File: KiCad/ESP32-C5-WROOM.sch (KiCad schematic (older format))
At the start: 4 parts, among them J14 USB_C_Receptacle_USB2.0, U13 ESP32-C5-WROOM-1U-N8R8

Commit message: Change R4 to 0603 and route the SD_LED circuit, add push-button for ESP32-C5 BOOT functionality (BT3)
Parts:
- added BT3: BT_Push, SF2000:Sunrom_Tactile_Switch_3x4x2mm_SMD_2-Pin, symbol Switch:SW_Push
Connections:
- net GND: now also BT3.1
- net at U13.15 (IO28): now also BT3.2
- no-connect marks 20 -> 19
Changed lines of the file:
@@
 NoConn ~ 1650 2550
 NoConn ~ 1650 2650
-NoConn ~ 1650 2950
 NoConn ~ 1650 3050
 NoConn ~ 1650 3150
 NoConn ~ 1650 3250
 NoConn ~ 1650 3350
+$Comp
+L Switch:SW_Push BT?
+U 1 1 6B13C84E
+P 950 2950
+AR Path="/6AFE5B10/6B13C84E" Ref="BT?"  Part="1"
+AR Path="/6AB92870/6B13C84E" Ref="BT3"  Part="1"
+F 0 "BT3" H 950 3235 50  0000 C CNN
+F 1 "BT_Push" H 950 3144 50  0000 C CNN
+F 2 "SF2000:Sunrom_Tactile_Switch_3x4x2mm_SMD_2-Pin" H 950 3150 50  0001 C CNN
+F 3 "~" H 950 3150 50  0001 C CNN
+	1    950  2950
+	1    0    0    -1
+$EndComp
+Text GLabel 750  2950 0    50   Input ~ 0
+GND
+Wire Wire Line
+	1650 2950 1150 2950
 $EndSCHEMATC

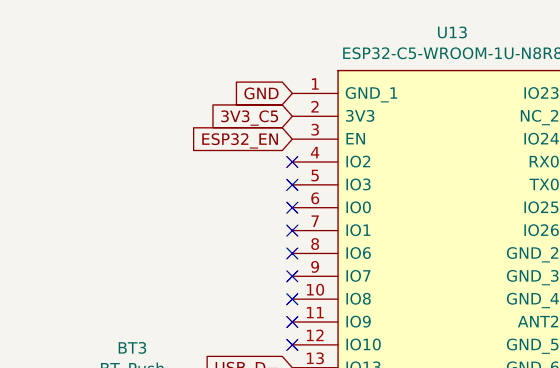
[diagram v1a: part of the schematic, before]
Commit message: Add BT4 push-button for RESET on the EN-signal for the ESP32-C5
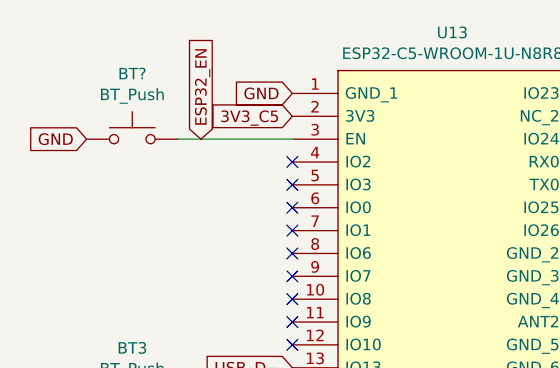
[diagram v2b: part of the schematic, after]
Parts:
- added BT?: BT_Push, SF2000:Sunrom_Tactile_Switch_3x4x2mm_SMD_2-Pin, symbol Switch:SW_Push
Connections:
- net ESP32_EN: now also BT?.2
- net GND: now also BT?.1
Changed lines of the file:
@@
 Text GLabel 3050 1550 2    50   Output ~ 0
 ESP32_TX1
-Text GLabel 1650 1750 0    50   Input ~ 0
+Text GLabel 1250 1750 1    50   Input ~ 0
 ESP32_EN
 NoConn ~ 3050 2550
@@
 Wire Wire Line
 	1650 2950 1150 2950
+$Comp
+L Switch:SW_Push BT?
+U 1 1 6B1C0633
+P 950 1750
+AR Path="/6AFE5B10/6B1C0633" Ref="BT?"  Part="1"
+AR Path="/6AB92870/6B1C0633" Ref="BT?"  Part="1"
+F 0 "BT?" H 950 2035 50  0000 C CNN
+F 1 "BT_Push" H 950 1944 50  0000 C CNN
+F 2 "SF2000:Sunrom_Tactile_Switch_3x4x2mm_SMD_2-Pin" H 950 1950 50  0001 C CNN
+F 3 "~" H 950 1950 50  0001 C CNN
+	1    950  1750
+	1    0    0    -1
+$EndComp
+Text GLabel 750  1750 0    50   Input ~ 0
+GND
+Wire Wire Line
+	1650 1750 1150 1750
 $EndSCHEMATC

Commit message: Change C15 to 0603 and use it for ESP32-C5 EN-signal, add 10k pull-up resistor (R24) on EN-signal
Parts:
- added C15: 0.1uF, Capacitor_SMD:C_0603_1608Metric_Pad1.08x0.95mm_HandSolder, symbol Device:C
- added R24: 10k, Resistor_SMD:R_0603_1608Metric_Pad0.98x0.95mm_HandSolder, symbol Device:R_Small
- gave numbers to parts that had none: 1
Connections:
- net ESP32_EN: now also C15.1, R24.1
- net GND: now also C15.2
- new net 3V3: R24.2
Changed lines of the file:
@@
 P 950 1750
 AR Path="/6AFE5B10/6B1C0633" Ref="BT?"  Part="1"
-AR Path="/6AB92870/6B1C0633" Ref="BT?"  Part="1"
-F 0 "BT?" H 950 2035 50  0000 C CNN
+AR Path="/6AB92870/6B1C0633" Ref="BT4"  Part="1"
+F 0 "BT4" H 950 2035 50  0000 C CNN
 F 1 "BT_Push" H 950 1944 50  0000 C CNN
 F 2 "SF2000:Sunrom_Tactile_Switch_3x4x2mm_SMD_2-Pin" H 950 1950 50  0001 C CNN
@@
 GND
 Wire Wire Line
-	1650 1750 1150 1750
+	1650 1750 1400 1750
+$Comp
+L Device:C C?
+U 1 1 6B1E6F7D
+P 1400 1900
+AR Path="/6B1E6F7D" Ref="C?"  Part="1"
+AR Path="/620D263D/6B1E6F7D" Ref="C?"  Part="1"
+AR Path="/6AB92870/6B1E6F7D" Ref="C15"  Part="1"
+F 0 "C15" H 1450 2000 50  0000 L CNN
+F 1 "0.1uF" H 1400 1800 50  0000 L CNN
+F 2 "Capacitor_SMD:C_0603_1608Metric_Pad1.08x0.95mm_HandSolder" H 1438 1750 50  0001 C CNN
+F 3 "~" H 1400 1900 50  0001 C CNN
+	1    1400 1900
+	1    0    0    -1
+$EndComp
+Text GLabel 1400 2050 3    50   Input ~ 0
+GND
+$Comp
+L Device:R_Small R?
+U 1 1 6B1F631E
+P 1150 1850
+AR Path="/6B1F631E" Ref="R?"  Part="1"
+AR Path="/6AFE5B10/6B1F631E" Ref="R?"  Part="1"
+AR Path="/6AB92870/6B1F631E" Ref="R24"  Part="1"
+F 0 "R24" H 1000 1850 50  0000 L CNN
+F 1 "10k" H 950 1750 50  0000 L CNN
+F 2 "Resistor_SMD:R_0603_1608Metric_Pad0.98x0.95mm_HandSolder" H 1150 1850 50  0001 C CNN
+F 3 "~" H 1150 1850 50  0001 C CNN
+	1    1150 1850
+	1    0    0    -1
+$EndComp
+Text GLabel 1150 2000 3    50   Input ~ 0
+3V3
+Wire Wire Line
+	1150 1950 1150 2000
+Connection ~ 1400 1750
+Connection ~ 1150 1750
+Wire Wire Line
+	1150 1750 1400 1750
 $EndSCHEMATC

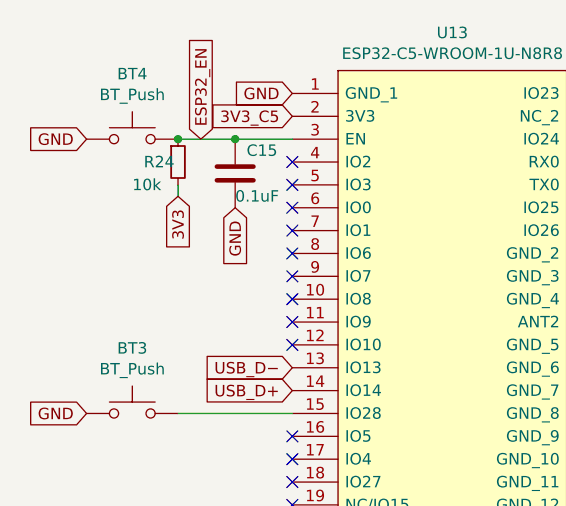
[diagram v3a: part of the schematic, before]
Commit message: Assign 3V3_C5 to R24 pull-up resistor, place and route C11, C15, C46, R24 on underside of ESP32-C5 module.
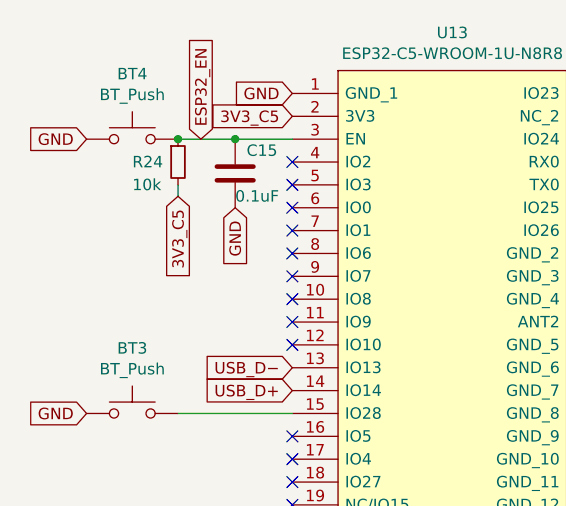
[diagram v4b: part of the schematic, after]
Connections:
- net 3V3 is gone; now on net 3V3_C5: R24.2
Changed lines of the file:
@@
 AR Path="/6AFE5B10/6B1F631E" Ref="R?"  Part="1"
 AR Path="/6AB92870/6B1F631E" Ref="R24"  Part="1"
-F 0 "R24" H 1000 1850 50  0000 L CNN
+F 0 "R24" H 950 1850 50  0000 L CNN
 F 1 "10k" H 950 1750 50  0000 L CNN
 F 2 "Resistor_SMD:R_0603_1608Metric_Pad0.98x0.95mm_HandSolder" H 1150 1850 50  0001 C CNN
@@
 $EndComp
 Text GLabel 1150 2000 3    50   Input ~ 0
-3V3
+3V3_C5
 Wire Wire Line
 	1150 1950 1150 2000

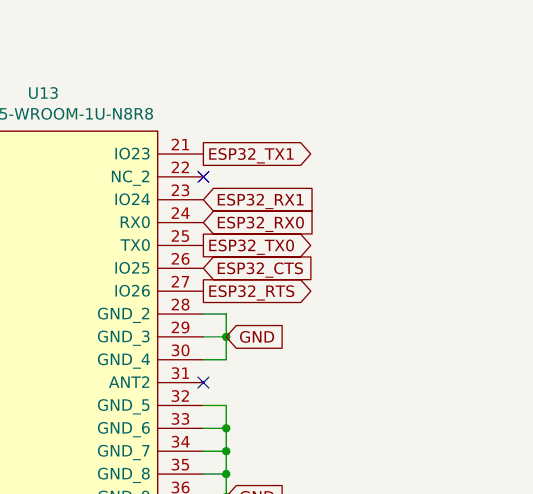
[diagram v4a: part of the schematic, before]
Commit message: Breakout UART0 (TX0,RX0) for the ESP32-C5  odule and put SMD pads on the underside for debugging purposes, Change C47 value from 0.01uF to 0.1uF, Swap position of C37 and C48.
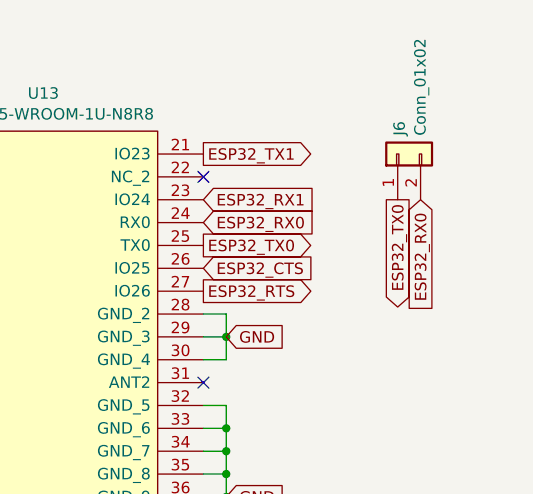
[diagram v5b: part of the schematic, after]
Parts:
- added J6: Conn_01x02, Connector_PinHeader_2.54mm:PinHeader_1x02_P2.54mm_Vertical, symbol Connector_Generic:Conn_01x02
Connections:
- net ESP32_RX0: now also J6.2 (Pin_2)
- net ESP32_TX0: now also J6.1 (Pin_1)
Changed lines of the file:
@@
 Wire Wire Line
 	1150 1750 1400 1750
+$Comp
+L Connector_Generic:Conn_01x02 J6
+U 1 1 6B744C51
+P 3900 1550
+F 0 "J6" H 3980 1542 50  0000 L CNN
+F 1 "Conn_01x02" H 3980 1451 50  0000 L CNN
+F 2 "Connector_PinHeader_2.54mm:PinHeader_1x02_P2.54mm_Vertical" H 3900 1550 50  0001 C CNN
+F 3 "~" H 3900 1550 50  0001 C CNN
+	1    3900 1550
+	0    -1   -1   0
+$EndComp
+Text GLabel 3900 1750 3    50   Output ~ 0
+ESP32_TX0
+Text GLabel 4000 1750 3    50   Input ~ 0
+ESP32_RX0
 $EndSCHEMATC

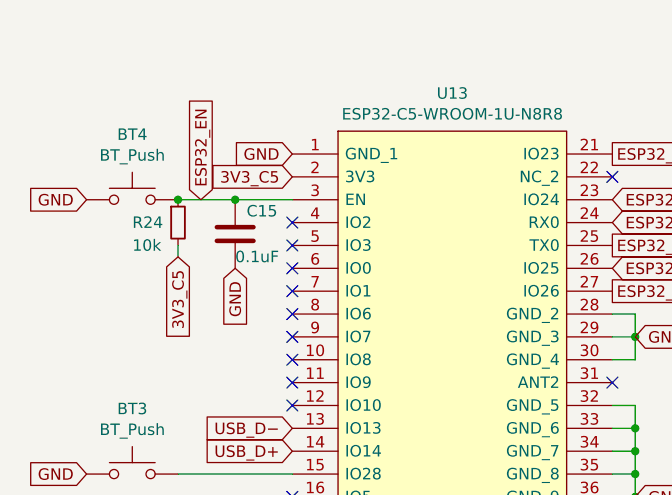
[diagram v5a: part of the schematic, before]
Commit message: Change C15 reference to C46, Change C11 reference to C15, Change C10 reference to C11, Change C46 reference to C10.
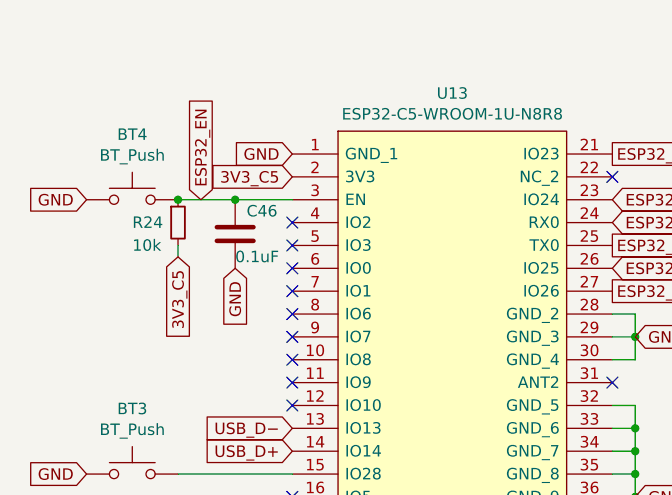
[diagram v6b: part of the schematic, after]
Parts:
- renumbered C15 to C46
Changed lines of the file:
@@
 AR Path="/6B1E6F7D" Ref="C?"  Part="1"
 AR Path="/620D263D/6B1E6F7D" Ref="C?"  Part="1"
-AR Path="/6AB92870/6B1E6F7D" Ref="C15"  Part="1"
-F 0 "C15" H 1450 2000 50  0000 L CNN
+AR Path="/6AB92870/6B1E6F7D" Ref="C46"  Part="1"
+F 0 "C46" H 1450 2000 50  0000 L CNN
 F 1 "0.1uF" H 1400 1800 50  0000 L CNN
 F 2 "Capacitor_SMD:C_0603_1608Metric_Pad1.08x0.95mm_HandSolder" H 1438 1750 50  0001 C CNN

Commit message: Change R8 reference to R11, Change R11 reference to R8, Change R11 reference to R21,Change R10 reference to R11,Change R9 reference to R10,Change R21 reference to R9.
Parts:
- renumbered R9 to R10, R10 to R11
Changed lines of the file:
@@
 3V3_C5
 $Comp
-L Device:R_Small R10
+L Device:R_Small R11
 U 1 1 6AEB9B3F
 P 2850 5250
-F 0 "R10" V 2750 5150 50  0000 L CNN
+F 0 "R11" V 2750 5150 50  0000 L CNN
 F 1 "5k1" V 2850 5200 50  0000 L CNN
 F 2 "Resistor_SMD:R_0603_1608Metric_Pad0.98x0.95mm_HandSolder" H 2850 5250 50  0001 C CNN
@@
 GND
 $Comp
-L Device:R_Small R9
+L Device:R_Small R10
 U 1 1 6AEC8E87
 P 2950 5250
-F 0 "R9" V 3050 5150 50  0000 L CNN
+F 0 "R10" V 3050 5150 50  0000 L CNN
 F 1 "5k1" V 2950 5200 50  0000 L CNN
 F 2 "Resistor_SMD:R_0603_1608Metric_Pad0.98x0.95mm_HandSolder" H 2950 5250 50  0001 C CNN

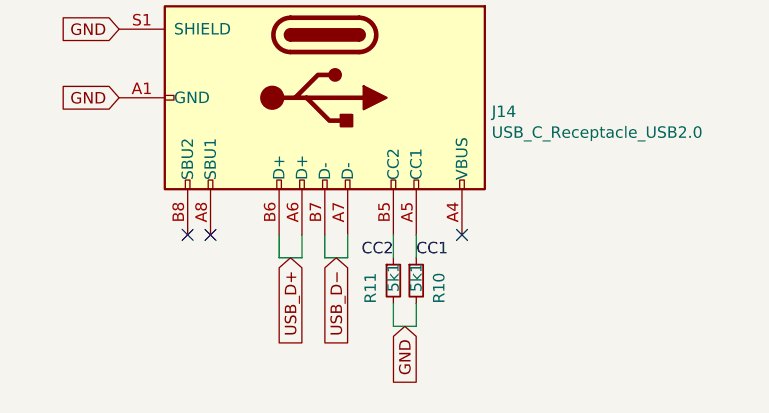
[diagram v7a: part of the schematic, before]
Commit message: Change R11 reference to R18, Change R10 reference to R17, Change R9 reference to R11, Change R18 reference to R10, Change R17 reference to R9.
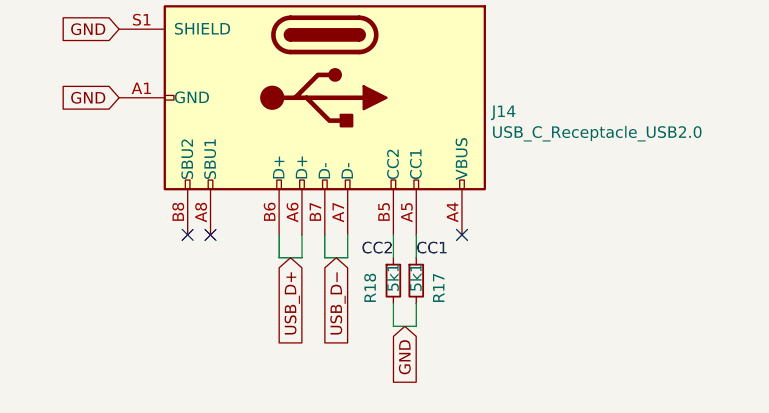
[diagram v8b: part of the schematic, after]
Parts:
- renumbered R10 to R17, R11 to R18
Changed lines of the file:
@@
 3V3_C5
 $Comp
-L Device:R_Small R11
+L Device:R_Small R18
 U 1 1 6AEB9B3F
 P 2850 5250
-F 0 "R11" V 2750 5150 50  0000 L CNN
+F 0 "R18" V 2750 5150 50  0000 L CNN
 F 1 "5k1" V 2850 5200 50  0000 L CNN
 F 2 "Resistor_SMD:R_0603_1608Metric_Pad0.98x0.95mm_HandSolder" H 2850 5250 50  0001 C CNN
@@
 GND
 $Comp
-L Device:R_Small R10
+L Device:R_Small R17
 U 1 1 6AEC8E87
 P 2950 5250
-F 0 "R10" V 3050 5150 50  0000 L CNN
+F 0 "R17" V 3050 5150 50  0000 L CNN
 F 1 "5k1" V 2950 5200 50  0000 L CNN
 F 2 "Resistor_SMD:R_0603_1608Metric_Pad0.98x0.95mm_HandSolder" H 2950 5250 50  0001 C CNN
